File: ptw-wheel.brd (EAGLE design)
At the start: 64 x 45 mm, 5 parts

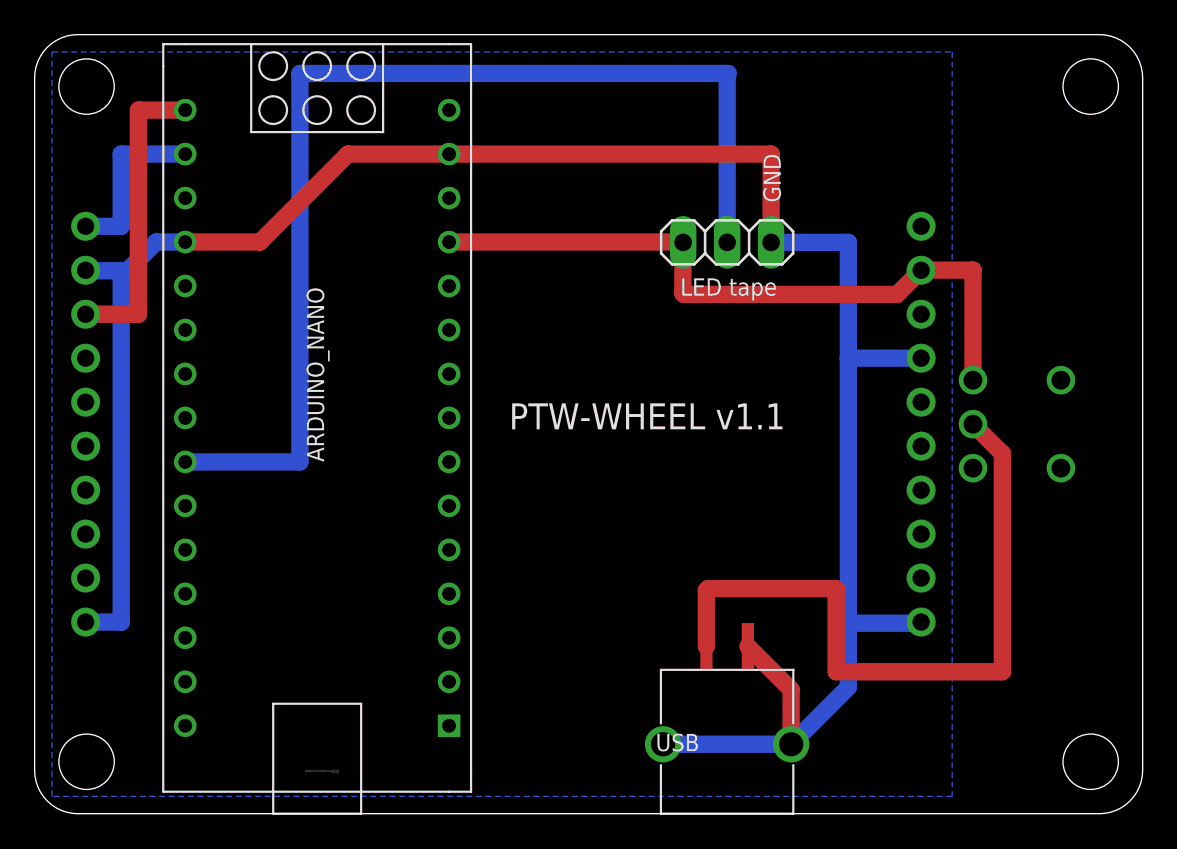
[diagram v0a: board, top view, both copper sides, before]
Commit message: Modify texts
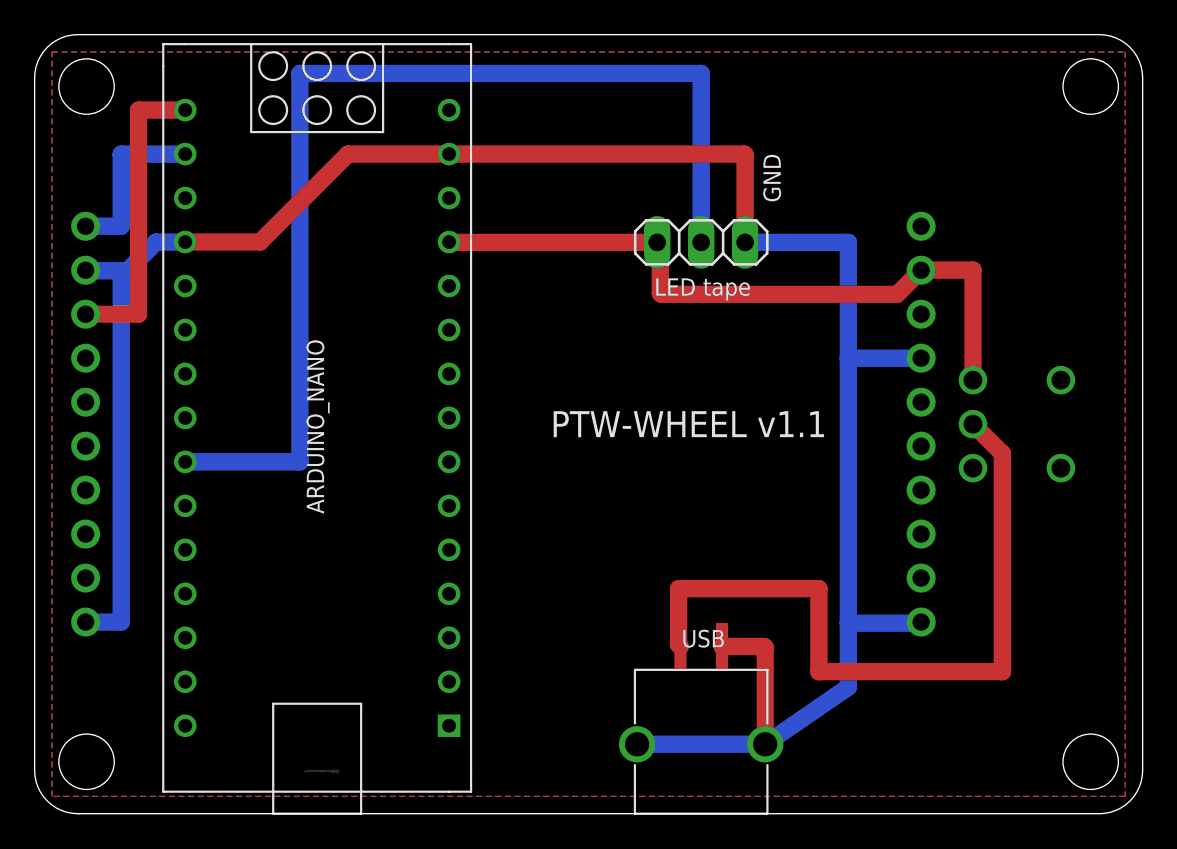
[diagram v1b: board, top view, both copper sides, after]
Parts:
- moved JP1 1.50 mm to (38.5, 33.0)
- moved USB 1.50 mm to (38.5, 8.31)
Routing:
- net GND: track 127.2 -> 129.8 mm
- net N$1: track 40.2 -> 41.9 mm
- net N$3: track 63.6 -> 62.0 mm
- added copper zone on layer 1, net GND
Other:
- board text added: "OFF"
- board text added: "ON"
- board text added: "POWER"
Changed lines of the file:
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@@
 <layers>
 <layer number="1" name="Top" color="4" fill="1" visible="yes" active="yes"/>
-<layer number="16" name="Bottom" color="1" fill="1" visible="no" active="yes"/>
+<layer number="16" name="Bottom" color="1" fill="1" visible="yes" active="yes"/>
 <layer number="17" name="Pads" color="2" fill="1" visible="yes" active="yes"/>
 <layer number="18" name="Vias" color="2" fill="1" visible="yes" active="yes"/>
@@
 <layer number="20" name="Dimension" color="24" fill="1" visible="yes" active="yes"/>
 <layer number="21" name="tPlace" color="7" fill="1" visible="yes" active="yes"/>
-<layer number="22" name="bPlace" color="7" fill="1" visible="yes" active="yes"/>
+<layer number="22" name="bPlace" color="7" fill="1" visible="no" active="yes"/>
 <layer number="23" name="tOrigins" color="15" fill="1" visible="yes" active="yes"/>
 <layer number="24" name="bOrigins" color="15" fill="1" visible="yes" active="yes"/>
 <layer number="25" name="tNames" color="7" fill="1" visible="yes" active="yes"/>
-<layer number="26" name="bNames" color="7" fill="1" visible="yes" active="yes"/>
-<layer number="27" name="tValues" color="7" fill="1" visible="no" active="yes"/>
+<layer number="26" name="bNames" color="7" fill="1" visible="no" active="yes"/>
+<layer number="27" name="tValues" color="7" fill="1" visible="yes" active="yes"/>
 <layer number="28" name="bValues" color="7" fill="1" visible="no" active="yes"/>
 <layer number="29" name="tStop" color="7" fill="3" visible="no" active="yes"/>
@@
 <layer number="49" name="Reference" color="7" fill="1" visible="yes" active="yes"/>
 <layer number="50" name="dxf" color="12" fill="1" visible="no" active="no"/>
-<layer number="51" name="tDocu" color="7" fill="1" visible="yes" active="yes"/>
-<layer number="52" name="bDocu" color="7" fill="1" visible="yes" active="yes"/>
+<layer number="51" name="tDocu" color="7" fill="1" visible="no" active="yes"/>
+<layer number="52" name="bDocu" color="7" fill="1" visible="no" active="yes"/>
 <layer number="53" name="tGND_GNDA" color="7" fill="9" visible="no" active="no"/>
 <layer number="54" name="bGND_GNDA" color="1" fill="9" visible="no" active="no"/>
@@
 <hole x="61" y="3" drill="3.2"/>
 <hole x="61" y="42" drill="3.2"/>
-<text x="27.4" y="22.2" size="1.5" layer="25">PTW-WHEEL v1.1</text>
-<text x="43.1" y="35.3" size="1" layer="25" rot="R90">GND</text>
+<text x="29.8" y="22.5" size="1.5" layer="25" font="vector" ratio="10" align="center-left">PTW-WHEEL v1.1</text>
+<text x="43.1" y="35.3" size="1" layer="25" font="vector" rot="R90">GND</text>
+<text x="62" y="15" size="1" layer="27" font="vector" align="center-right">ON</text>
+<text x="62" y="22.5" size="1" layer="27" font="vector" align="center-right">POWER</text>
+<text x="62" y="30" size="1" layer="27" font="vector" align="center-right">OFF</text>
 </plain>
 <attributes>
@@
 <elements>
 <element name="ARDUINO_NANO" library="ArduinoNanoV30" package="ARDUINO_NANO" value="" x="16.32" y="25.4" smashed="yes" rot="R90">
-<attribute name="NAME" x="16.72" y="20.32" size="1" layer="21" font="vector" rot="R90"/>
+<attribute name="NAME" x="16.72" y="17.32" size="1" layer="21" font="vector" rot="R90"/>
 <attribute name="VALUE" x="20.86" y="7.62" size="1.27" layer="21" font="vector" rot="R90"/>
 </element>
-<element name="JP1" library="pinhead" library_urn="urn:adsk.eagle:library:325" package="1X03" package3d_urn="urn:adsk.eagle:package:22458/2" value="LED tape" x="40" y="33" smashed="yes">
-<attribute name="VALUE" x="37.29" y="29.925" size="1" layer="25"/>
+<element name="JP1" library="pinhead" library_urn="urn:adsk.eagle:library:325" package="1X03" package3d_urn="urn:adsk.eagle:package:22458/2" value="LED tape" x="38.5" y="33" smashed="yes">
+<attribute name="VALUE" x="35.79" y="29.925" size="1" layer="25" font="vector"/>
 </element>
 <element name="KONASHI" library="konashiv2" package="KONASHI" value="KONASHI2.0" x="1" y="6" smashed="yes"/>
-<element name="USB" library="usbcon" package="USBCON" value="USBCON" x="40" y="8.31" smashed="yes" rot="R180">
-<attribute name="NAME" x="38.4" y="4.61" size="1" layer="25" rot="R180"/>
+<element name="USB" library="usbcon" package="USBCON" value="USBCON" x="38.5" y="8.31" smashed="yes" rot="R180">
+<attribute name="NAME" x="39.9" y="10.61" size="1" layer="25" font="vector" rot="R180"/>
 </element>
-<element name="U$1" library="toggle-switch" package="MTS-12PB-5P" value="MTS-12PB-5P" x="54.2" y="22.5" smashed="yes" rot="MR0">
-<attribute name="VALUE" x="59.669" y="27.918" size="1.27" layer="28" rot="MR0" align="center"/>
-</element>
+<element name="U$1" library="toggle-switch" package="MTS-12PB-5P" value="MTS-12PB-5P" x="54.2" y="22.5" smashed="yes" rot="MR0"/>
 </elements>
 <signals>
@@
 <wire x1="8.7" y1="20.32" x2="15.32668125" y2="20.32" width="1" layer="16"/>
 <wire x1="15.32668125" y1="42.75648125" x2="15.32668125" y2="20.32" width="1" layer="16"/>
-<wire x1="15.32668125" y1="42.75648125" x2="40" y2="42.75648125" width="1" layer="16"/>
-<wire x1="40" y1="42.75648125" x2="40.071040625" y2="42.75648125" width="1" layer="16"/>
-<wire x1="40" y1="33" x2="40" y2="42.75648125" width="1" layer="16"/>
+<wire x1="15.32668125" y1="42.75648125" x2="38.5" y2="42.75648125" width="1" layer="16"/>
+<wire x1="38.5" y1="33" x2="38.5" y2="42.75648125" width="1" layer="16"/>
 </signal>
 <signal name="N$4">
@@
 <wire x1="51.205640625" y1="31.389840625" x2="49.8158" y2="30" width="1" layer="1"/>
 <contactref element="U$1" pad="3"/>
-<wire x1="23.94" y1="33.02" x2="37.44" y2="33.02" width="1" layer="1"/>
-<wire x1="37.44" y1="33.02" x2="37.46" y2="33" width="1" layer="1"/>
-<wire x1="49.8158" y1="30" x2="37.5" y2="30" width="1" layer="1"/>
-<wire x1="37.5" y1="30" x2="37.44" y2="30.06" width="1" layer="1"/>
-<wire x1="37.44" y1="30.06" x2="37.44" y2="33.02" width="1" layer="1"/>
+<wire x1="36.14" y1="33.00243125" x2="35.96" y2="33" width="1" layer="1"/>
+<wire x1="49.8158" y1="30" x2="36.2" y2="30" width="1" layer="1"/>
+<wire x1="36.2" y1="30" x2="36.14" y2="30.06" width="1" layer="1"/>
+<wire x1="36.14" y1="30.06" x2="36.14" y2="33.00243125" width="1" layer="1"/>
 <wire x1="54.2" y1="25.04" x2="54.2" y2="31.4" width="1" layer="1"/>
 <wire x1="54.2" y1="31.4" x2="51.2158" y2="31.4" width="1" layer="1"/>
 <wire x1="51.2158" y1="31.4" x2="51.205640625" y2="31.389840625" width="1" layer="1"/>
+<wire x1="35.96" y1="33" x2="23.96" y2="33" width="1" layer="1"/>
+<wire x1="23.96" y1="33" x2="23.94" y2="33.02" width="1" layer="1"/>
 </signal>
 <signal name="GND">
@@
 <wire x1="13.02" y1="33.02" x2="18.1" y2="38.1" width="1" layer="1"/>
 <wire x1="18.1" y1="38.1" x2="23.94" y2="38.1" width="1" layer="1"/>
-<wire x1="36.3" y1="4.01" x2="43.7" y2="4.01" width="1" layer="16"/>
-<polygon width="1" layer="16">
-<vertex x="1" y="44"/>
-<vertex x="53" y="44"/>
-<vertex x="53" y="1"/>
-<vertex x="1" y="1"/>
-</polygon>
+<wire x1="34.8" y1="4.01" x2="42.2" y2="4.01" width="1" layer="16"/>
 <wire x1="5.36" y1="31.36" x2="5" y2="31.36" width="1" layer="16"/>
 <wire x1="5" y1="31.36" x2="2.97548125" y2="31.36" width="1" layer="16"/>
 <wire x1="2.97548125" y1="31.36" x2="2.945640625" y2="31.389840625" width="1" layer="16"/>
 <wire x1="2.945640625" y1="11.069840625" x2="5" y2="11.069840625" width="1" layer="16"/>
-<wire x1="42.54" y1="33" x2="47" y2="33" width="1" layer="16"/>
+<wire x1="41.04" y1="33" x2="47" y2="33" width="1" layer="16"/>
 <wire x1="47" y1="33" x2="47" y2="26.3" width="1" layer="16"/>
 <wire x1="47" y1="26.3" x2="47" y2="11" width="1" layer="16"/>
@@
 <wire x1="51.205640625" y1="11.069840625" x2="51.1358" y2="11" width="1" layer="16"/>
 <wire x1="51.1358" y1="11" x2="47" y2="11" width="1" layer="16"/>
-<wire x1="43.7" y1="4.01" x2="47" y2="7.31" width="1" layer="16"/>
+<wire x1="42.2" y1="4.01" x2="47" y2="7.31" width="1" layer="16"/>
 <wire x1="47" y1="11" x2="47" y2="7.31" width="1" layer="16"/>
-<wire x1="42.54" y1="33" x2="42.54" y2="38.1" width="1" layer="1"/>
-<wire x1="42.54" y1="38.1" x2="23.94" y2="38.1" width="1" layer="1"/>
-<wire x1="41.2" y1="9.66" x2="43.7" y2="7.16" width="1" layer="1"/>
-<wire x1="43.7" y1="7.16" x2="43.7" y2="4.01" width="1" layer="1"/>
+<wire x1="42.2" y1="4.01" x2="42.2" y2="9.6" width="1" layer="1"/>
+<wire x1="42.2" y1="9.6" x2="42.14" y2="9.66" width="1" layer="1"/>
+<wire x1="42.14" y1="9.66" x2="39.7" y2="9.66" width="1" layer="1"/>
+<wire x1="23.94" y1="38.1" x2="41" y2="38.1" width="1" layer="1"/>
+<wire x1="41" y1="38.1" x2="41.04" y2="38.06" width="1" layer="1"/>
+<wire x1="41.04" y1="38.06" x2="41.04" y2="33" width="1" layer="1"/>
+<polygon width="1" layer="1">
+<vertex x="1" y="44"/>
+<vertex x="63" y="44"/>
+<vertex x="63" y="1"/>
+<vertex x="1" y="1"/>
+</polygon>
+<polygon width="1" layer="16">
+<vertex x="1" y="44"/>
+<vertex x="63" y="44"/>
+<vertex x="63" y="1"/>
+<vertex x="1" y="1"/>
+</polygon>
 </signal>
 <signal name="N$1">
@@
 <wire x1="54.2" y1="22.5" x2="55.9" y2="20.8" width="1" layer="1"/>
 <wire x1="55.9" y1="20.8" x2="55.9" y2="8.2" width="1" layer="1"/>
-<wire x1="55.9" y1="8.2" x2="46.3" y2="8.2" width="1" layer="1"/>
-<wire x1="46.3" y1="8.2" x2="46.3" y2="13" width="1" layer="1"/>
-<wire x1="46.3" y1="13" x2="38.9" y2="13" width="1" layer="1"/>
-<wire x1="38.9" y1="13" x2="38.8" y2="12.9" width="1" layer="1"/>
-<wire x1="38.8" y1="12.9" x2="38.8" y2="9.66" width="1" layer="1"/>
+<wire x1="55.9" y1="8.2" x2="45.3" y2="8.2" width="1" layer="1"/>
+<wire x1="45.3" y1="8.2" x2="45.3" y2="13" width="1" layer="1"/>
+<wire x1="45.3" y1="13" x2="37.2" y2="13" width="1" layer="1"/>
+<wire x1="37.2" y1="13" x2="37.2" y2="9.76" width="1" layer="1"/>
+<wire x1="37.2" y1="9.76" x2="37.3" y2="9.66" width="1" layer="1"/>
 </signal>
 </signals>
